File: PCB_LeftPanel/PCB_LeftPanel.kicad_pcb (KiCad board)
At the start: 2 copper layers, 149.2 x 215.9 mm, 234 parts, among them J1 USB_B, J10 HDR_2x8, J11 HDR_2x8, J12 HDR_2x8, J13 HDR_2x8, J14 HDR_2x8, J15 HDR_2x8, J16 HDR_2x8, J17 HDR_2x8, J18 HDR_2x8, J19 HDR_2x8, J2 AVR-ISP-6, J20 HDR_2x8, J21 HDR_2x8, J22 HDR_2x8, J23 HDR_2x8, J24 Conn_01x03, J25 Conn_01x03, J26 Conn_01x03, J27 Conn_01x03, J28 Conn_01x03, J29 Conn_01x03, J3 Jack-DC, J30 Conn_01x03, J31 Conn_01x03, J32 DB9_Female, J36 Conn_01x08_Male, J4 HDR_2x8, J5 HDR_2x8, J6 HDR_2x8, J7 HDR_2x8, J8 HDR_2x8, J9 HDR_2x8, U1 ATmega16-16PU, U2 7442, U3 MCP2200-I-SO, U4 74AHC04, U5 74AHC04, Y1 Crystal

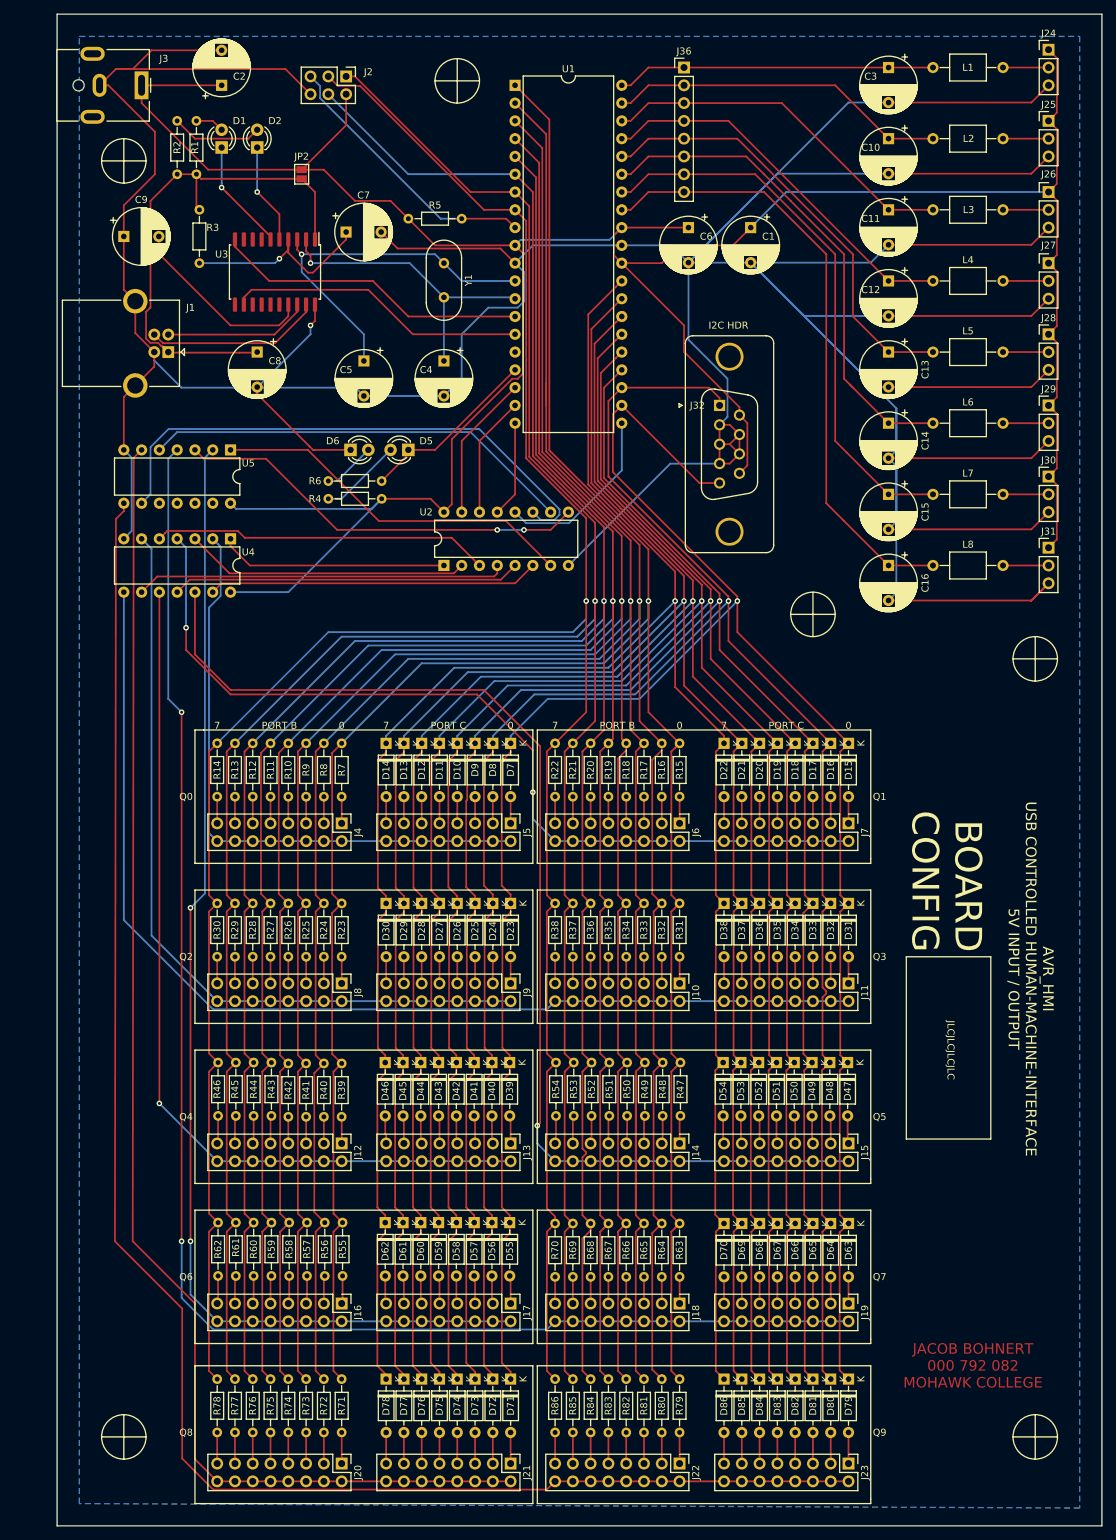
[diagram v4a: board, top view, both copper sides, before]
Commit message: Add files via upload
Update to Revision 4.A
Board now based on Arduino Leonardo / Uno
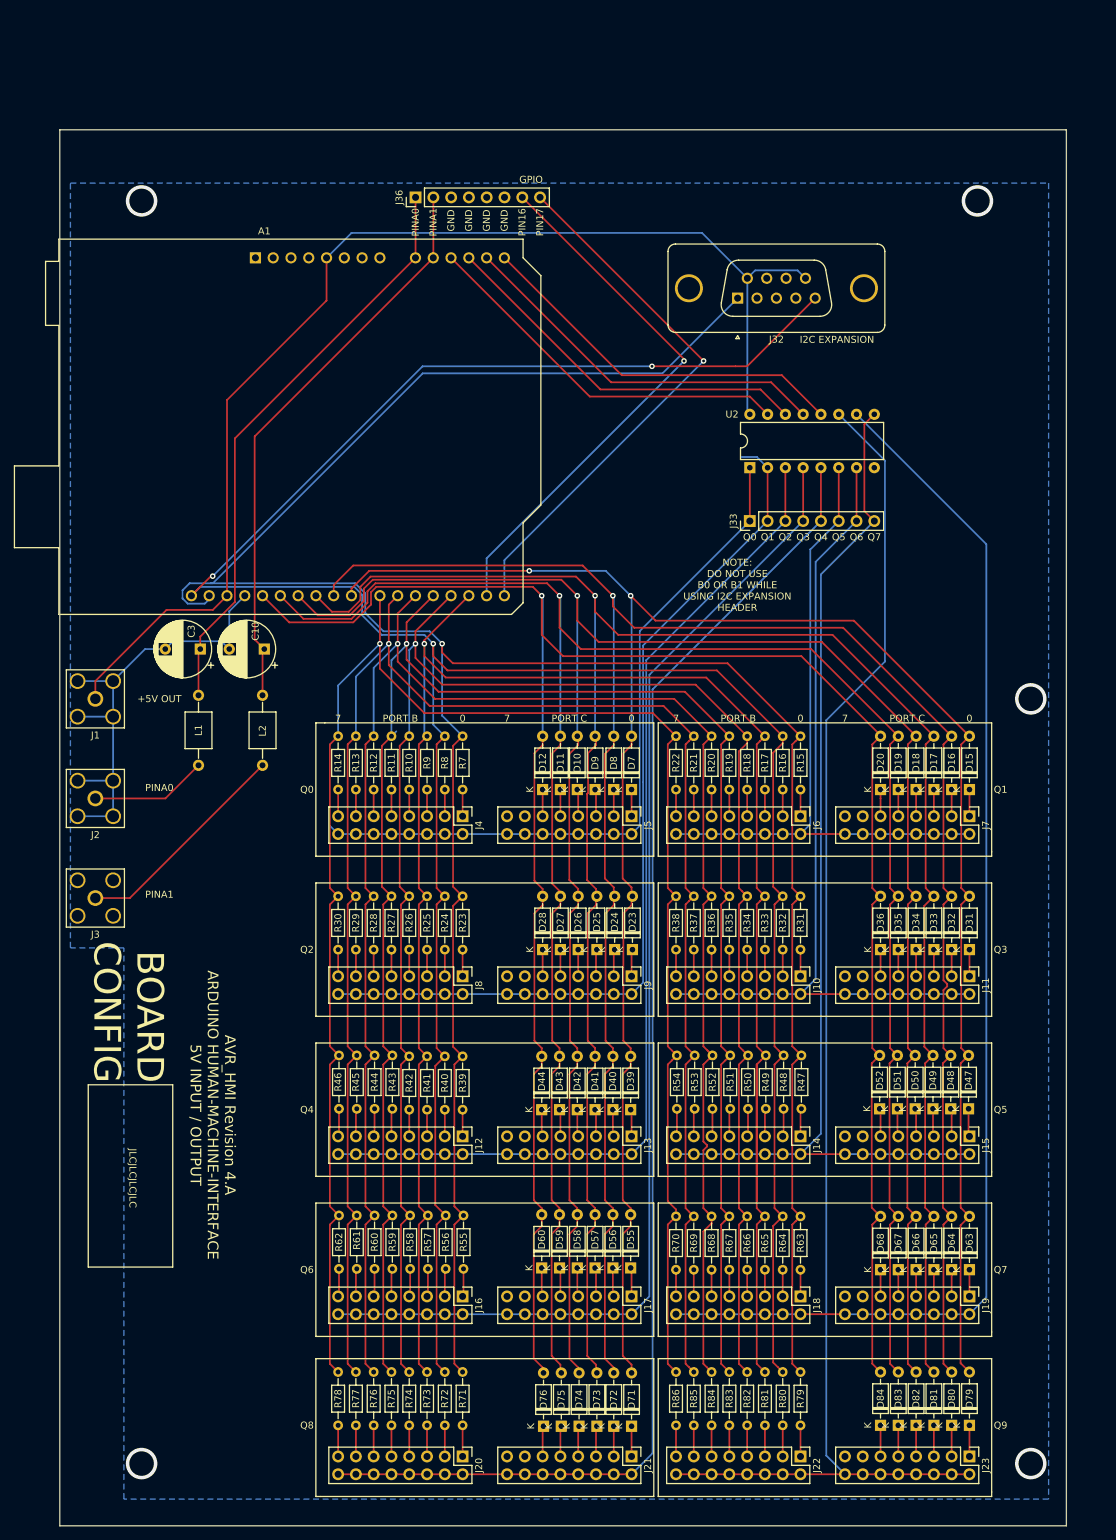
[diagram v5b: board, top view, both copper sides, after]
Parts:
- removed C1, C11, C12, C13, C14, C15, C16, C7, C8: 100nF, Capacitor_THT:CP_Radial_D8.0mm_P5.00mm
- removed C2: 270uF, Capacitor_THT:CP_Radial_D8.0mm_P5.00mm
- removed C4, C5: 22pF, Capacitor_THT:CP_Radial_D8.0mm_P5.00mm
- removed C6: 100nf, Capacitor_THT:CP_Radial_D8.0mm_P5.00mm
- removed C9: 0.22uF, Capacitor_THT:CP_Radial_D8.0mm_P5.00mm
- removed D1, D2, D5, D6: LED, LED_THT:LED_D3.0mm
- removed D13, D14, D21, D22, D29, D30, D37, D38, D45, D46, D53, D54, D61, D62, D69, D70, D77, D78, D85, D86: 1N4148, Diode_THT:D_DO-35_SOD27_P7.62mm_Horizontal
- removed J24, J25, J26, J27, J28, J29, J30, J31: Conn_01x03, Connector_PinHeader_2.54mm:PinHeader_1x03_P2.54mm_Vertical
- removed JP2: Solder Bridge, Jumper:SolderJumper-2_P1.3mm_Open_Pad1.0x1.5mm
- removed L3, L4, L5, L6, L7, L8: 4uH, Inductor_THT:L_Axial_L5.0mm_D3.6mm_P10.00mm_Horizontal_Murata_BL01RN1A2A2
- removed R1, R2, R4, R6: 560Ω, Resistor_THT:R_Axial_DIN0204_L3.6mm_D1.6mm_P7.62mm_Horizontal
- removed R3: 10KΩ, Resistor_THT:R_Axial_DIN0204_L3.6mm_D1.6mm_P7.62mm_Horizontal
- removed R5: 100k, Resistor_THT:R_Axial_DIN0204_L3.6mm_D1.6mm_P7.62mm_Horizontal
- removed U1: ATmega16-16PU, Package_DIP:DIP-40_W15.24mm
- removed U3: MCP2200-I-SO, Package_SO:SOIC-20W_7.5x12.8mm_P1.27mm
- removed U4, U5: 74AHC04, Package_DIP:DIP-14_W7.62mm
- removed Y1: Crystal, Crystal:Crystal_HC49-4H_Vertical
- added A1: Arduino_Leonardo, Module:Arduino_UNO_R3, F.Cu at (56.9, 53.8)
- added J33: Conn_01x08, Connector_PinHeader_2.54mm:PinHeader_1x08_P2.54mm_Vertical, F.Cu at (127.5, 91.4)
- J1: value USB_B -> Conn_Coaxial; footprint Connector_USB:USB_B_OST_USB-B1HSxx_Horizontal -> Connector_Coaxial:SMA_Amphenol_132203-12_Horizontal
- J2: value AVR-ISP-6 -> Conn_Coaxial; footprint Connector_PinHeader_2.54mm:PinHeader_2x03_P2.54mm_Vertical -> Connector_Coaxial:SMA_Amphenol_132203-12_Horizontal
- J3: value Jack-DC -> Conn_Coaxial; footprint Connector_BarrelJack:BarrelJack_CUI_PJ-063AH_Horizontal -> Connector_Coaxial:SMA_Amphenol_132203-12_Horizontal
- moved L1 138.0 mm to (48.8, 116.3), turned to -90 degrees
- moved C3 128.7 mm to (49.0, 109.7), turned to 180 degrees
- moved L2 124.5 mm to (57.9, 116.3), turned to -90 degrees
- moved J3 116.3 mm to (34.0, 145.3), turned to 90 degrees
- moved C10 115.2 mm to (58.2, 109.7), turned to 180 degrees
- moved J2 109.2 mm to (34.0, 131.1), turned to 90 degrees
- moved J1 50.6 mm to (34.0, 116.8), turned to 90 degrees
- moved U2 45.9 mm to (127.5, 83.8)
- moved J36 42.6 mm to (79.8, 45.2), turned to 90 degrees
- moved D73 18.7 mm to (105.7, 220.7), turned to 90 degrees
- moved D74 18.7 mm to (103.1, 220.7), turned to 90 degrees
- moved D75 18.7 mm to (100.6, 220.7), turned to 90 degrees
- moved D76 18.7 mm to (98.0, 220.7), turned to 90 degrees
- moved D23 18.6 mm to (110.7, 152.7), turned to 90 degrees
- moved D25 18.6 mm to (105.7, 152.7), turned to 90 degrees
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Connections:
- net /InputOutputPins/PB2 renamed PB2
- net /InputOutputPins/PB3 renamed PB3
- net /InputOutputPins/PB4 renamed PB4
- D10 pad 1: /InputOutputPins/PC3 -> Net-(D10-Pad1)
- D10 pad 2: Net-(D10-Pad2) -> PC3
- D11 pad 1: /InputOutputPins/PC4 -> Net-(D11-Pad1)
- D11 pad 2: Net-(D11-Pad2) -> PC4
- D12 pad 1: /InputOutputPins/PC5 -> Net-(D12-Pad1)
- D12 pad 2: Net-(D12-Pad2) -> PC5
- D15 pad 1: /InputOutputPins/PC0 -> Net-(D15-Pad1)
- D15 pad 2: Net-(D15-Pad2) -> PC0
- D16 pad 1: /InputOutputPins/PC1 -> Net-(D16-Pad1)
- D16 pad 2: Net-(D16-Pad2) -> PC1
- D17 pad 1: /InputOutputPins/PC2 -> Net-(D17-Pad1)
- D17 pad 2: Net-(D17-Pad2) -> PC2
- D18 pad 1: /InputOutputPins/PC3 -> Net-(D18-Pad1)
- D18 pad 2: Net-(D18-Pad2) -> PC3
- D19 pad 1: /InputOutputPins/PC4 -> Net-(D19-Pad1)
- D19 pad 2: Net-(D19-Pad2) -> PC4
- D20 pad 1: /InputOutputPins/PC5 -> Net-(D20-Pad1)
- D20 pad 2: Net-(D20-Pad2) -> PC5
- D23 pad 1: /InputOutputPins/PC0 -> Net-(D23-Pad1)
- D23 pad 2: Net-(D23-Pad2) -> PC0
- D24 pad 1: /InputOutputPins/PC1 -> Net-(D24-Pad1)
- D24 pad 2: Net-(D24-Pad2) -> PC1
- D25 pad 1: /InputOutputPins/PC2 -> Net-(D25-Pad1)
- D25 pad 2: Net-(D25-Pad2) -> PC2
- D26 pad 1: /InputOutputPins/PC3 -> Net-(D26-Pad1)
- D26 pad 2: Net-(D26-Pad2) -> PC3
- D27 pad 1: /InputOutputPins/PC4 -> Net-(D27-Pad1)
- D27 pad 2: Net-(D27-Pad2) -> PC4
- D28 pad 1: /InputOutputPins/PC5 -> Net-(D28-Pad1)
- D28 pad 2: Net-(D28-Pad2) -> PC5
- D31 pad 1: /InputOutputPins/PC0 -> Net-(D31-Pad1)
- D31 pad 2: Net-(D31-Pad2) -> PC0
- D32 pad 1: /InputOutputPins/PC1 -> Net-(D32-Pad1)
- D32 pad 2: Net-(D32-Pad2) -> PC1
- D33 pad 1: /InputOutputPins/PC2 -> Net-(D33-Pad1)
- D33 pad 2: Net-(D33-Pad2) -> PC2
- D34 pad 1: /InputOutputPins/PC3 -> Net-(D34-Pad1)
- D34 pad 2: Net-(D34-Pad2) -> PC3
- D35 pad 1: /InputOutputPins/PC4 -> Net-(D35-Pad1)
- D35 pad 2: Net-(D35-Pad2) -> PC4
- D36 pad 1: /InputOutputPins/PC5 -> Net-(D36-Pad1)
- D36 pad 2: Net-(D36-Pad2) -> PC5
- D39 pad 1: /InputOutputPins/PC0 -> Net-(D39-Pad1)
- D39 pad 2: Net-(D39-Pad2) -> PC0
- D40 pad 1: /InputOutputPins/PC1 -> Net-(D40-Pad1)
- D40 pad 2: Net-(D40-Pad2) -> PC1
- D41 pad 1: /InputOutputPins/PC2 -> Net-(D41-Pad1)
- D41 pad 2: Net-(D41-Pad2) -> PC2
- D42 pad 1: /InputOutputPins/PC3 -> Net-(D42-Pad1)
- D42 pad 2: Net-(D42-Pad2) -> PC3
- D43 pad 1: /InputOutputPins/PC4 -> Net-(D43-Pad1)
- D43 pad 2: Net-(D43-Pad2) -> PC4
- D44 pad 1: /InputOutputPins/PC5 -> Net-(D44-Pad1)
- D44 pad 2: Net-(D44-Pad2) -> PC5
- D47 pad 1: /InputOutputPins/PC0 -> Net-(D47-Pad1)
- D47 pad 2: Net-(D47-Pad2) -> PC0
- D48 pad 1: /InputOutputPins/PC1 -> Net-(D48-Pad1)
- D48 pad 2: Net-(D48-Pad2) -> PC1
- D49 pad 1: /InputOutputPins/PC2 -> Net-(D49-Pad1)
- D49 pad 2: Net-(D49-Pad2) -> PC2
- D50 pad 1: /InputOutputPins/PC3 -> Net-(D50-Pad1)
- D50 pad 2: Net-(D50-Pad2) -> PC3
- D51 pad 1: /InputOutputPins/PC4 -> Net-(D51-Pad1)
- D51 pad 2: Net-(D51-Pad2) -> PC4
- D52 pad 1: /InputOutputPins/PC5 -> Net-(D52-Pad1)
- D52 pad 2: Net-(D52-Pad2) -> PC5
- D55 pad 1: /InputOutputPins/PC0 -> Net-(D55-Pad1)
- D55 pad 2: Net-(D55-Pad2) -> PC0
- D56 pad 1: /InputOutputPins/PC1 -> Net-(D56-Pad1)
- D56 pad 2: Net-(D56-Pad2) -> PC1
- D57 pad 1: /InputOutputPins/PC2 -> Net-(D57-Pad1)
- D57 pad 2: Net-(D57-Pad2) -> PC2
- D58 pad 1: /InputOutputPins/PC3 -> Net-(D58-Pad1)
- D58 pad 2: Net-(D58-Pad2) -> PC3
- D59 pad 1: /InputOutputPins/PC4 -> Net-(D59-Pad1)
- D59 pad 2: Net-(D59-Pad2) -> PC4
- D60 pad 1: /InputOutputPins/PC5 -> Net-(D60-Pad1)
- D60 pad 2: Net-(D60-Pad2) -> PC5
- D63 pad 1: /InputOutputPins/PC0 -> Net-(D63-Pad1)
- D63 pad 2: Net-(D63-Pad2) -> PC0
- D64 pad 1: /InputOutputPins/PC1 -> Net-(D64-Pad1)
- D64 pad 2: Net-(D64-Pad2) -> PC1
- D65 pad 1: /InputOutputPins/PC2 -> Net-(D65-Pad1)
- D65 pad 2: Net-(D65-Pad2) -> PC2
- D66 pad 1: /InputOutputPins/PC3 -> Net-(D66-Pad1)
- D66 pad 2: Net-(D66-Pad2) -> PC3
- D67 pad 1: /InputOutputPins/PC4 -> Net-(D67-Pad1)
- D67 pad 2: Net-(D67-Pad2) -> PC4
- D68 pad 1: /InputOutputPins/PC5 -> Net-(D68-Pad1)
- D68 pad 2: Net-(D68-Pad2) -> PC5
- D7 pad 1: /InputOutputPins/PC0 -> Net-(D7-Pad1)
- D7 pad 2: Net-(D7-Pad2) -> PC0
- D71 pad 1: /InputOutputPins/PC0 -> Net-(D71-Pad1)
- D71 pad 2: Net-(D71-Pad2) -> PC0
- D72 pad 1: /InputOutputPins/PC1 -> Net-(D72-Pad1)
- D72 pad 2: Net-(D72-Pad2) -> PC1
- D73 pad 1: /InputOutputPins/PC2 -> Net-(D73-Pad1)
- D73 pad 2: Net-(D73-Pad2) -> PC2
- D74 pad 1: /InputOutputPins/PC3 -> Net-(D74-Pad1)
- D74 pad 2: Net-(D74-Pad2) -> PC3
- D75 pad 1: /InputOutputPins/PC4 -> Net-(D75-Pad1)
- D75 pad 2: Net-(D75-Pad2) -> PC4
- D76 pad 1: /InputOutputPins/PC5 -> Net-(D76-Pad1)
- D76 pad 2: Net-(D76-Pad2) -> PC5
- D79 pad 1: /InputOutputPins/PC0 -> Net-(D79-Pad1)
- D79 pad 2: Net-(D79-Pad2) -> PC0
- D8 pad 1: /InputOutputPins/PC1 -> Net-(D8-Pad1)
- D8 pad 2: Net-(D8-Pad2) -> PC1
- D80 pad 1: /InputOutputPins/PC1 -> Net-(D80-Pad1)
- D80 pad 2: Net-(D80-Pad2) -> PC1
- D81 pad 1: /InputOutputPins/PC2 -> Net-(D81-Pad1)
- D81 pad 2: Net-(D81-Pad2) -> PC2
- D82 pad 1: /InputOutputPins/PC3 -> Net-(D82-Pad1)
- D82 pad 2: Net-(D82-Pad2) -> PC3
- D83 pad 1: /InputOutputPins/PC4 -> Net-(D83-Pad1)
- D83 pad 2: Net-(D83-Pad2) -> PC4
- D84 pad 1: /InputOutputPins/PC5 -> Net-(D84-Pad1)
- D84 pad 2: Net-(D84-Pad2) -> PC5
- D9 pad 1: /InputOutputPins/PC2 -> Net-(D9-Pad1)
- D9 pad 2: Net-(D9-Pad2) -> PC2
- J1 pad 1: VBUS -> +5V
- J1 pad 2: Net-(J1-Pad2) -> GND
- J10 pad 10: Net-(J10-Pad10) -> Q6
- J10 pad 12: Net-(J10-Pad10) -> Q6
- J10 pad 14: Net-(J10-Pad10) -> Q6
- J10 pad 16: Net-(J10-Pad10) -> Q6
- J10 pad 2: Net-(J10-Pad10) -> Q6
- J10 pad 4: Net-(J10-Pad10) -> Q6
- J10 pad 6: Net-(J10-Pad10) -> Q6
- J10 pad 8: Net-(J10-Pad10) -> Q6
- J11 pad 1: Net-(D31-Pad2) -> Net-(D31-Pad1)
- J11 pad 10: Net-(J10-Pad10) -> Q6
- J11 pad 11: Net-(D36-Pad2) -> Net-(D36-Pad1)
- J11 pad 12: Net-(J10-Pad10) -> Q6
- J11 pad 13: Net-(D37-Pad2) -> GND
- J11 pad 14: Net-(J10-Pad10) -> Q6
- J11 pad 15: Net-(D38-Pad2) -> GND
- J11 pad 16: Net-(J10-Pad10) -> Q6
- J11 pad 2: Net-(J10-Pad10) -> Q6
- J11 pad 3: Net-(D32-Pad2) -> Net-(D32-Pad1)
- J11 pad 4: Net-(J10-Pad10) -> Q6
- J11 pad 5: Net-(D33-Pad2) -> Net-(D33-Pad1)
- J11 pad 6: Net-(J10-Pad10) -> Q6
- J11 pad 7: Net-(D34-Pad2) -> Net-(D34-Pad1)
- J11 pad 8: Net-(J10-Pad10) -> Q6
- J11 pad 9: Net-(D35-Pad2) -> Net-(D35-Pad1)
- J12 pad 10: Net-(J12-Pad10) -> Q2
- J12 pad 12: Net-(J12-Pad10) -> Q2
- J12 pad 14: Net-(J12-Pad10) -> Q2
- J12 pad 16: Net-(J12-Pad10) -> Q2
- J12 pad 2: Net-(J12-Pad10) -> Q2
- J12 pad 4: Net-(J12-Pad10) -> Q2
- J12 pad 6: Net-(J12-Pad10) -> Q2
- J12 pad 8: Net-(J12-Pad10) -> Q2
- J13 pad 1: Net-(D39-Pad2) -> Net-(D39-Pad1)
- J13 pad 10: Net-(J12-Pad10) -> Q2
- J13 pad 11: Net-(D44-Pad2) -> Net-(D44-Pad1)
- J13 pad 12: Net-(J12-Pad10) -> Q2
- J13 pad 13: Net-(D45-Pad2) -> GND
- J13 pad 14: Net-(J12-Pad10) -> Q2
- J13 pad 15: Net-(D46-Pad2) -> GND
- J13 pad 16: Net-(J12-Pad10) -> Q2
- J13 pad 2: Net-(J12-Pad10) -> Q2
- J13 pad 3: Net-(D40-Pad2) -> Net-(D40-Pad1)
- J13 pad 4: Net-(J12-Pad10) -> Q2
- J13 pad 5: Net-(D41-Pad2) -> Net-(D41-Pad1)
- J13 pad 6: Net-(J12-Pad10) -> Q2
- J13 pad 7: Net-(D42-Pad2) -> Net-(D42-Pad1)
- J13 pad 8: Net-(J12-Pad10) -> Q2
- J13 pad 9: Net-(D43-Pad2) -> Net-(D43-Pad1)
- J14 pad 10: Net-(J14-Pad10) -> Q7
- J14 pad 12: Net-(J14-Pad10) -> Q7
- J14 pad 14: Net-(J14-Pad10) -> Q7
- J14 pad 16: Net-(J14-Pad10) -> Q7
- J14 pad 2: Net-(J14-Pad10) -> Q7
- J14 pad 4: Net-(J14-Pad10) -> Q7
- J14 pad 6: Net-(J14-Pad10) -> Q7
- J14 pad 8: Net-(J14-Pad10) -> Q7
- J15 pad 1: Net-(D47-Pad2) -> Net-(D47-Pad1)
- J15 pad 10: Net-(J14-Pad10) -> Q7
- J15 pad 11: Net-(D52-Pad2) -> Net-(D52-Pad1)
- J15 pad 12: Net-(J14-Pad10) -> Q7
- J15 pad 13: Net-(D53-Pad2) -> GND
- J15 pad 14: Net-(J14-Pad10) -> Q7
- J15 pad 15: Net-(D54-Pad2) -> GND
- J15 pad 16: Net-(J14-Pad10) -> Q7
- J15 pad 2: Net-(J14-Pad10) -> Q7
- J15 pad 3: Net-(D48-Pad2) -> Net-(D48-Pad1)
- J15 pad 4: Net-(J14-Pad10) -> Q7
- J15 pad 5: Net-(D49-Pad2) -> Net-(D49-Pad1)
- J15 pad 6: Net-(J14-Pad10) -> Q7
- J15 pad 7: Net-(D50-Pad2) -> Net-(D50-Pad1)
- J15 pad 8: Net-(J14-Pad10) -> Q7
- J15 pad 9: Net-(D51-Pad2) -> Net-(D51-Pad1)
- J16 pad 10: Net-(J16-Pad10) -> Q3
- J16 pad 12: Net-(J16-Pad10) -> Q3
- J16 pad 14: Net-(J16-Pad10) -> Q3
- J16 pad 16: Net-(J16-Pad10) -> Q3
- J16 pad 2: Net-(J16-Pad10) -> Q3
- J16 pad 4: Net-(J16-Pad10) -> Q3
- J16 pad 6: Net-(J16-Pad10) -> Q3
- J16 pad 8: Net-(J16-Pad10) -> Q3
- J17 pad 1: Net-(D55-Pad2) -> Net-(D55-Pad1)
- J17 pad 10: Net-(J16-Pad10) -> Q3
- J17 pad 11: Net-(D60-Pad2) -> Net-(D60-Pad1)
- J17 pad 12: Net-(J16-Pad10) -> Q3
- J17 pad 13: Net-(D61-Pad2) -> GND
- J17 pad 14: Net-(J16-Pad10) -> Q3
- J17 pad 15: Net-(D62-Pad2) -> GND
- J17 pad 16: Net-(J16-Pad10) -> Q3
- J17 pad 2: Net-(J16-Pad10) -> Q3
- J17 pad 3: Net-(D56-Pad2) -> Net-(D56-Pad1)
- J17 pad 4: Net-(J16-Pad10) -> Q3
- J17 pad 5: Net-(D57-Pad2) -> Net-(D57-Pad1)
- J17 pad 6: Net-(J16-Pad10) -> Q3
- J17 pad 7: Net-(D58-Pad2) -> Net-(D58-Pad1)
- J17 pad 8: Net-(J16-Pad10) -> Q3
- J17 pad 9: Net-(D59-Pad2) -> Net-(D59-Pad1)
- J18 pad 10: Net-(J18-Pad10) -> Q8
- J18 pad 12: Net-(J18-Pad10) -> Q8
- J18 pad 14: Net-(J18-Pad10) -> Q8
- J18 pad 16: Net-(J18-Pad10) -> Q8
- J18 pad 2: Net-(J18-Pad10) -> Q8
- J18 pad 4: Net-(J18-Pad10) -> Q8
- J18 pad 6: Net-(J18-Pad10) -> Q8
- J18 pad 8: Net-(J18-Pad10) -> Q8
- J19 pad 1: Net-(D63-Pad2) -> Net-(D63-Pad1)
- J19 pad 10: Net-(J18-Pad10) -> Q8
- J19 pad 11: Net-(D68-Pad2) -> Net-(D68-Pad1)
- J19 pad 12: Net-(J18-Pad10) -> Q8
- J19 pad 13: Net-(D69-Pad2) -> GND
- J19 pad 14: Net-(J18-Pad10) -> Q8
- J19 pad 15: Net-(D70-Pad2) -> GND
- J19 pad 16: Net-(J18-Pad10) -> Q8
- J19 pad 2: Net-(J18-Pad10) -> Q8
- J19 pad 3: Net-(D64-Pad2) -> Net-(D64-Pad1)
- J19 pad 4: Net-(J18-Pad10) -> Q8
- J19 pad 5: Net-(D65-Pad2) -> Net-(D65-Pad1)
- J19 pad 6: Net-(J18-Pad10) -> Q8
- J19 pad 7: Net-(D66-Pad2) -> Net-(D66-Pad1)
- J19 pad 8: Net-(J18-Pad10) -> Q8
- J19 pad 9: Net-(D67-Pad2) -> Net-(D67-Pad1)
- J2 pad 1: /InputOutputPins/PB6 -> Net-(J2-Pad1)
- J2 pad 2: +5V -> GND
- J20 pad 10: Net-(J20-Pad10) -> Q4
- J20 pad 12: Net-(J20-Pad10) -> Q4
- J20 pad 14: Net-(J20-Pad10) -> Q4
- J20 pad 16: Net-(J20-Pad10) -> Q4
- J20 pad 2: Net-(J20-Pad10) -> Q4
- J20 pad 4: Net-(J20-Pad10) -> Q4
- J20 pad 6: Net-(J20-Pad10) -> Q4
- J20 pad 8: Net-(J20-Pad10) -> Q4
- J21 pad 1: Net-(D71-Pad2) -> Net-(D71-Pad1)
- J21 pad 10: Net-(J20-Pad10) -> Q4
- J21 pad 11: Net-(D76-Pad2) -> Net-(D76-Pad1)
- J21 pad 12: Net-(J20-Pad10) -> Q4
- J21 pad 13: Net-(D77-Pad2) -> GND
- J21 pad 14: Net-(J20-Pad10) -> Q4
- J21 pad 15: Net-(D78-Pad2) -> GND
- J21 pad 16: Net-(J20-Pad10) -> Q4
- J21 pad 2: Net-(J20-Pad10) -> Q4
- J21 pad 3: Net-(D72-Pad2) -> Net-(D72-Pad1)
- J21 pad 4: Net-(J20-Pad10) -> Q4
- J21 pad 5: Net-(D73-Pad2) -> Net-(D73-Pad1)
- J21 pad 6: Net-(J20-Pad10) -> Q4
- J21 pad 7: Net-(D74-Pad2) -> Net-(D74-Pad1)
- J21 pad 8: Net-(J20-Pad10) -> Q4
- J21 pad 9: Net-(D75-Pad2) -> Net-(D75-Pad1)
- J22 pad 10: Net-(J22-Pad10) -> Q9
- J22 pad 12: Net-(J22-Pad10) -> Q9
- J22 pad 14: Net-(J22-Pad10) -> Q9
- J22 pad 16: Net-(J22-Pad10) -> Q9
- J22 pad 2: Net-(J22-Pad10) -> Q9
- J22 pad 4: Net-(J22-Pad10) -> Q9
- J22 pad 6: Net-(J22-Pad10) -> Q9
- J22 pad 8: Net-(J22-Pad10) -> Q9
- J23 pad 1: Net-(D79-Pad2) -> Net-(D79-Pad1)
- J23 pad 10: Net-(J22-Pad10) -> Q9
- J23 pad 11: Net-(D84-Pad2) -> Net-(D84-Pad1)
- J23 pad 12: Net-(J22-Pad10) -> Q9
- J23 pad 13: Net-(D85-Pad2) -> GND
- J23 pad 14: Net-(J22-Pad10) -> Q9
- J23 pad 15: Net-(D86-Pad2) -> GND
- J23 pad 16: Net-(J22-Pad10) -> Q9
- J23 pad 2: Net-(J22-Pad10) -> Q9
- J23 pad 3: Net-(D80-Pad2) -> Net-(D80-Pad1)
- J23 pad 4: Net-(J22-Pad10) -> Q9
- J23 pad 5: Net-(D81-Pad2) -> Net-(D81-Pad1)
- J23 pad 6: Net-(J22-Pad10) -> Q9
- J23 pad 7: Net-(D82-Pad2) -> Net-(D82-Pad1)
- J23 pad 8: Net-(J22-Pad10) -> Q9
- J23 pad 9: Net-(D83-Pad2) -> Net-(D83-Pad1)
- J3 pad 1: +5V -> Net-(J3-Pad1)
- J32 pad 1: /InputOutputPins/PC1 -> /I2C Expansion Connector/SDA
- J32 pad 5: /InputOutputPins/PC0 -> /I2C Expansion Connector/SCL
- J36 pad 3: /Analog Inputs/PA2 -> GND
- J36 pad 4: /Analog Inputs/PA3 -> GND
- J36 pad 5: /Analog Inputs/PA4 -> GND
- J36 pad 6: /Analog Inputs/PA5 -> GND
- J36 pad 7: /Analog Inputs/PA6 -> RXD
- J36 pad 8: /Analog Inputs/PA7 -> TXD
- J4 pad 10: Net-(J4-Pad10) -> Q0
- J4 pad 12: Net-(J4-Pad10) -> Q0
- J4 pad 14: Net-(J4-Pad10) -> Q0
- J4 pad 16: Net-(J4-Pad10) -> Q0
- J4 pad 2: Net-(J4-Pad10) -> Q0
- J4 pad 4: Net-(J4-Pad10) -> Q0
- J4 pad 6: Net-(J4-Pad10) -> Q0
- J4 pad 8: Net-(J4-Pad10) -> Q0
- J5 pad 1: Net-(D7-Pad2) -> Net-(D7-Pad1)
- J5 pad 10: Net-(J4-Pad10) -> Q0
- J5 pad 11: Net-(D12-Pad2) -> Net-(D12-Pad1)
- J5 pad 12: Net-(J4-Pad10) -> Q0
- J5 pad 13: Net-(D13-Pad2) -> GND
- J5 pad 14: Net-(J4-Pad10) -> Q0
- J5 pad 15: Net-(D14-Pad2) -> GND
- J5 pad 16: Net-(J4-Pad10) -> Q0
- J5 pad 2: Net-(J4-Pad10) -> Q0
- J5 pad 3: Net-(D8-Pad2) -> Net-(D8-Pad1)
- J5 pad 4: Net-(J4-Pad10) -> Q0
- J5 pad 5: Net-(D9-Pad2) -> Net-(D9-Pad1)
- J5 pad 6: Net-(J4-Pad10) -> Q0
- J5 pad 7: Net-(D10-Pad2) -> Net-(D10-Pad1)
- J5 pad 8: Net-(J4-Pad10) -> Q0
- J5 pad 9: Net-(D11-Pad2) -> Net-(D11-Pad1)
- J6 pad 10: Net-(J6-Pad10) -> Q5
- J6 pad 12: Net-(J6-Pad10) -> Q5
- J6 pad 14: Net-(J6-Pad10) -> Q5
- J6 pad 16: Net-(J6-Pad10) -> Q5
- J6 pad 2: Net-(J6-Pad10) -> Q5
- J6 pad 4: Net-(J6-Pad10) -> Q5
- J6 pad 6: Net-(J6-Pad10) -> Q5
- J6 pad 8: Net-(J6-Pad10) -> Q5
- J7 pad 1: Net-(D15-Pad2) -> Net-(D15-Pad1)
- J7 pad 10: Net-(J6-Pad10) -> Q5
- J7 pad 11: Net-(D20-Pad2) -> Net-(D20-Pad1)
- J7 pad 12: Net-(J6-Pad10) -> Q5
- J7 pad 13: Net-(D21-Pad2) -> GND
- J7 pad 14: Net-(J6-Pad10) -> Q5
- J7 pad 15: Net-(D22-Pad2) -> GND
- J7 pad 16: Net-(J6-Pad10) -> Q5
- J7 pad 2: Net-(J6-Pad10) -> Q5
- J7 pad 3: Net-(D16-Pad2) -> Net-(D16-Pad1)
- J7 pad 4: Net-(J6-Pad10) -> Q5
- J7 pad 5: Net-(D17-Pad2) -> Net-(D17-Pad1)
- J7 pad 6: Net-(J6-Pad10) -> Q5
- J7 pad 7: Net-(D18-Pad2) -> Net-(D18-Pad1)
- J7 pad 8: Net-(J6-Pad10) -> Q5
- J7 pad 9: Net-(D19-Pad2) -> Net-(D19-Pad1)
- J8 pad 10: Net-(J8-Pad10) -> Q1
- J8 pad 12: Net-(J8-Pad10) -> Q1
- J8 pad 14: Net-(J8-Pad10) -> Q1
- J8 pad 16: Net-(J8-Pad10) -> Q1
- J8 pad 2: Net-(J8-Pad10) -> Q1
- J8 pad 4: Net-(J8-Pad10) -> Q1
- J8 pad 6: Net-(J8-Pad10) -> Q1
- J8 pad 8: Net-(J8-Pad10) -> Q1
- J9 pad 1: Net-(D23-Pad2) -> Net-(D23-Pad1)
- J9 pad 10: Net-(J8-Pad10) -> Q1
- J9 pad 11: Net-(D28-Pad2) -> Net-(D28-Pad1)
- J9 pad 12: Net-(J8-Pad10) -> Q1
- J9 pad 13: Net-(D29-Pad2) -> GND
- J9 pad 14: Net-(J8-Pad10) -> Q1
- J9 pad 15: Net-(D30-Pad2) -> GND
- J9 pad 16: Net-(J8-Pad10) -> Q1
- J9 pad 2: Net-(J8-Pad10) -> Q1
- J9 pad 3: Net-(D24-Pad2) -> Net-(D24-Pad1)
- J9 pad 4: Net-(J8-Pad10) -> Q1
- J9 pad 5: Net-(D25-Pad2) -> Net-(D25-Pad1)
- J9 pad 6: Net-(J8-Pad10) -> Q1
- J9 pad 7: Net-(D26-Pad2) -> Net-(D26-Pad1)
- J9 pad 8: Net-(J8-Pad10) -> Q1
- J9 pad 9: Net-(D27-Pad2) -> Net-(D27-Pad1)
- L1 pad 2: Net-(J24-Pad2) -> Net-(J2-Pad1)
- L2 pad 2: Net-(J25-Pad2) -> Net-(J3-Pad1)
- R12 pad 2: /InputOutputPins/PB5 -> PB5
- R13 pad 2: /InputOutputPins/PB6 -> PB6
- R14 pad 2: /InputOutputPins/PB7 -> PB7
- R15 pad 2: /InputOutputPins/PB0 -> /I2C Expansion Connector/SDA
- R16 pad 2: /InputOutputPins/PB1 -> /I2C Expansion Connector/SCL
- R20 pad 2: /InputOutputPins/PB5 -> PB5
- R21 pad 2: /InputOutputPins/PB6 -> PB6
- R22 pad 2: /InputOutputPins/PB7 -> PB7
- R23 pad 2: /InputOutputPins/PB0 -> /I2C Expansion Connector/SDA
- R24 pad 2: /InputOutputPins/PB1 -> /I2C Expansion Connector/SCL
- R28 pad 2: /InputOutputPins/PB5 -> PB5
- R29 pad 2: /InputOutputPins/PB6 -> PB6
- R30 pad 2: /InputOutputPins/PB7 -> PB7
- R31 pad 2: /InputOutputPins/PB0 -> /I2C Expansion Connector/SDA
- R32 pad 2: /InputOutputPins/PB1 -> /I2C Expansion Connector/SCL
- R36 pad 2: /InputOutputPins/PB5 -> PB5
- R37 pad 2: /InputOutputPins/PB6 -> PB6
- R38 pad 2: /InputOutputPins/PB7 -> PB7
- R39 pad 2: /InputOutputPins/PB0 -> /I2C Expansion Connector/SDA
- R40 pad 2: /InputOutputPins/PB1 -> /I2C Expansion Connector/SCL
- R44 pad 2: /InputOutputPins/PB5 -> PB5
- R45 pad 2: /InputOutputPins/PB6 -> PB6
- R46 pad 2: /InputOutputPins/PB7 -> PB7
- R47 pad 2: /InputOutputPins/PB0 -> /I2C Expansion Connector/SDA
- R48 pad 2: /InputOutputPins/PB1 -> /I2C Expansion Connector/SCL
- R52 pad 2: /InputOutputPins/PB5 -> PB5
- R53 pad 2: /InputOutputPins/PB6 -> PB6
- R54 pad 2: /InputOutputPins/PB7 -> PB7
- R55 pad 2: /InputOutputPins/PB0 -> /I2C Expansion Connector/SDA
- R56 pad 2: /InputOutputPins/PB1 -> /I2C Expansion Connector/SCL
- R60 pad 2: /InputOutputPins/PB5 -> PB5
- R61 pad 2: /InputOutputPins/PB6 -> PB6
- R62 pad 2: /InputOutputPins/PB7 -> PB7
- R63 pad 2: /InputOutputPins/PB0 -> /I2C Expansion Connector/SDA
- R64 pad 2: /InputOutputPins/PB1 -> /I2C Expansion Connector/SCL
- R68 pad 2: /InputOutputPins/PB5 -> PB5
- R69 pad 2: /InputOutputPins/PB6 -> PB6
- R7 pad 2: /InputOutputPins/PB0 -> /I2C Expansion Connector/SDA
- R70 pad 2: /InputOutputPins/PB7 -> PB7
- R71 pad 2: /InputOutputPins/PB0 -> /I2C Expansion Connector/SDA
- R72 pad 2: /InputOutputPins/PB1 -> /I2C Expansion Connector/SCL
- R76 pad 2: /InputOutputPins/PB5 -> PB5
- R77 pad 2: /InputOutputPins/PB6 -> PB6
- R78 pad 2: /InputOutputPins/PB7 -> PB7
- R79 pad 2: /InputOutputPins/PB0 -> /I2C Expansion Connector/SDA
- R8 pad 2: /InputOutputPins/PB1 -> /I2C Expansion Connector/SCL
- R80 pad 2: /InputOutputPins/PB1 -> /I2C Expansion Connector/SCL
- R84 pad 2: /InputOutputPins/PB5 -> PB5
- R85 pad 2: /InputOutputPins/PB6 -> PB6
- R86 pad 2: /InputOutputPins/PB7 -> PB7
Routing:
- net GND: track 773.2 -> 67.6 mm, vias 1 -> 5
- net /I2C Expansion Connector/SCL: track 0.00 -> 407.2 mm, vias 0 -> 3
- net /I2C Expansion Connector/SDA: track 0.00 -> 402.6 mm, vias 0 -> 1
- net /InputOutputPins/PB7: track 369.1 -> 0.00 mm, vias 1 -> 0
- net /InputOutputPins/PB5: track 369.0 -> 0.00 mm, vias 1 -> 0
- net /InputOutputPins/PB6: track 366.8 -> 0.00 mm, vias 1 -> 0
- net /InputOutputPins/PB1: track 348.2 -> 0.00 mm, vias 1 -> 0
- net /InputOutputPins/PB0: track 347.4 -> 0.00 mm, vias 1 -> 0
- net /InputOutputPins/PC7: track 315.6 -> 0.00 mm, vias 1 -> 0
- net PC5: track 0.00 -> 314.6 mm, vias 0 -> 1
- net PC4: track 0.00 -> 313.8 mm, vias 0 -> 1
- net /InputOutputPins/PC1: track 313.7 -> 0.00 mm, vias 1 -> 0
- net PC3: track 0.00 -> 313.3 mm, vias 0 -> 1
- net /InputOutputPins/PC0: track 313.0 -> 0.00 mm, vias 1 -> 0
- net PC2: track 0.00 -> 312.8 mm, vias 0 -> 1
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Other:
- board size 149.2 x 215.9 mm -> 143.8 x 199.4 mm
- net class Default removed
- board text added: "+5V OUT"
- board text added: "AVR_HMI Revision 4.A ARDUINO HUMAN-MACHINE-INTERFACE 5V INPUT / OUTPUT"
- board text added: "GND"
- board text added: "GPIO"
- board text added: "I2C EXPANSION"
- board text added: "NOTE: DO NOT USE B0 OR B1 WHILE USING I2C EXPANSION HEADER"
- board text added: "PIN16"
- board text added: "PIN17"
- board text added: "PINA0"
- board text added: "PINA1"
- board text removed: "AVR_HMI USB CONTROLLED HUMAN-MACHINE-INTERFACE 5V INPUT / OUTPUT"
- board text removed: "JACOB BOHNERT 000 792 082 MOHAWK COLLEGE"

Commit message: Add files via upload
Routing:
- net PB2: track 287.1 -> 267.6 mm
- net Q1: track 129.6 -> 125.1 mm
- net Q0: track 102.9 -> 101.2 mm
- net PB4: track 266.3 -> 265.3 mm
- net GND: vias 5 -> 6
- added copper zone on F.Cu, net GND
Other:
- board size 143.8 x 199.4 mm -> 143.8 x 193 mm
